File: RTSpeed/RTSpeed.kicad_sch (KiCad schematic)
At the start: 40 parts, among them J1 SWD, J2 USB C Receptacle, J3 MOTOR, J4 POWER IN, SW1 NRST, SW2 BOOT0, SW3 USER, U4 STM32F411CEUx, U5 LM317, Y1 25MHz, Y2 32.768kHz

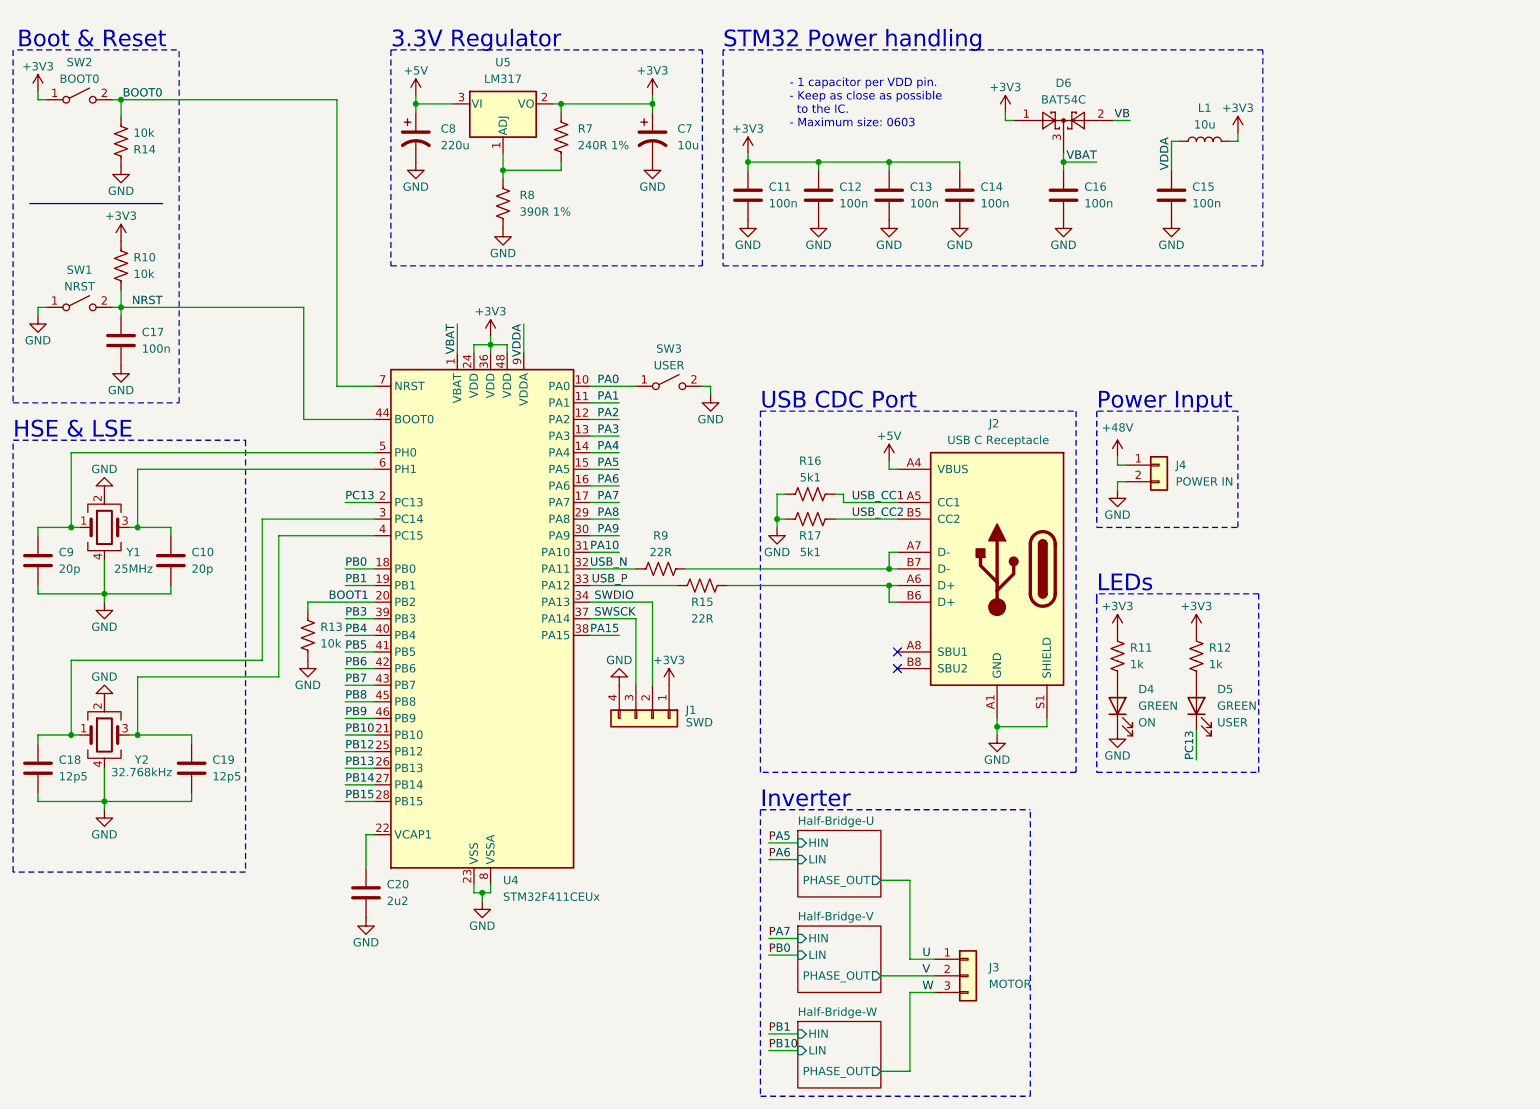
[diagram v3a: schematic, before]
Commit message: Added some footprints
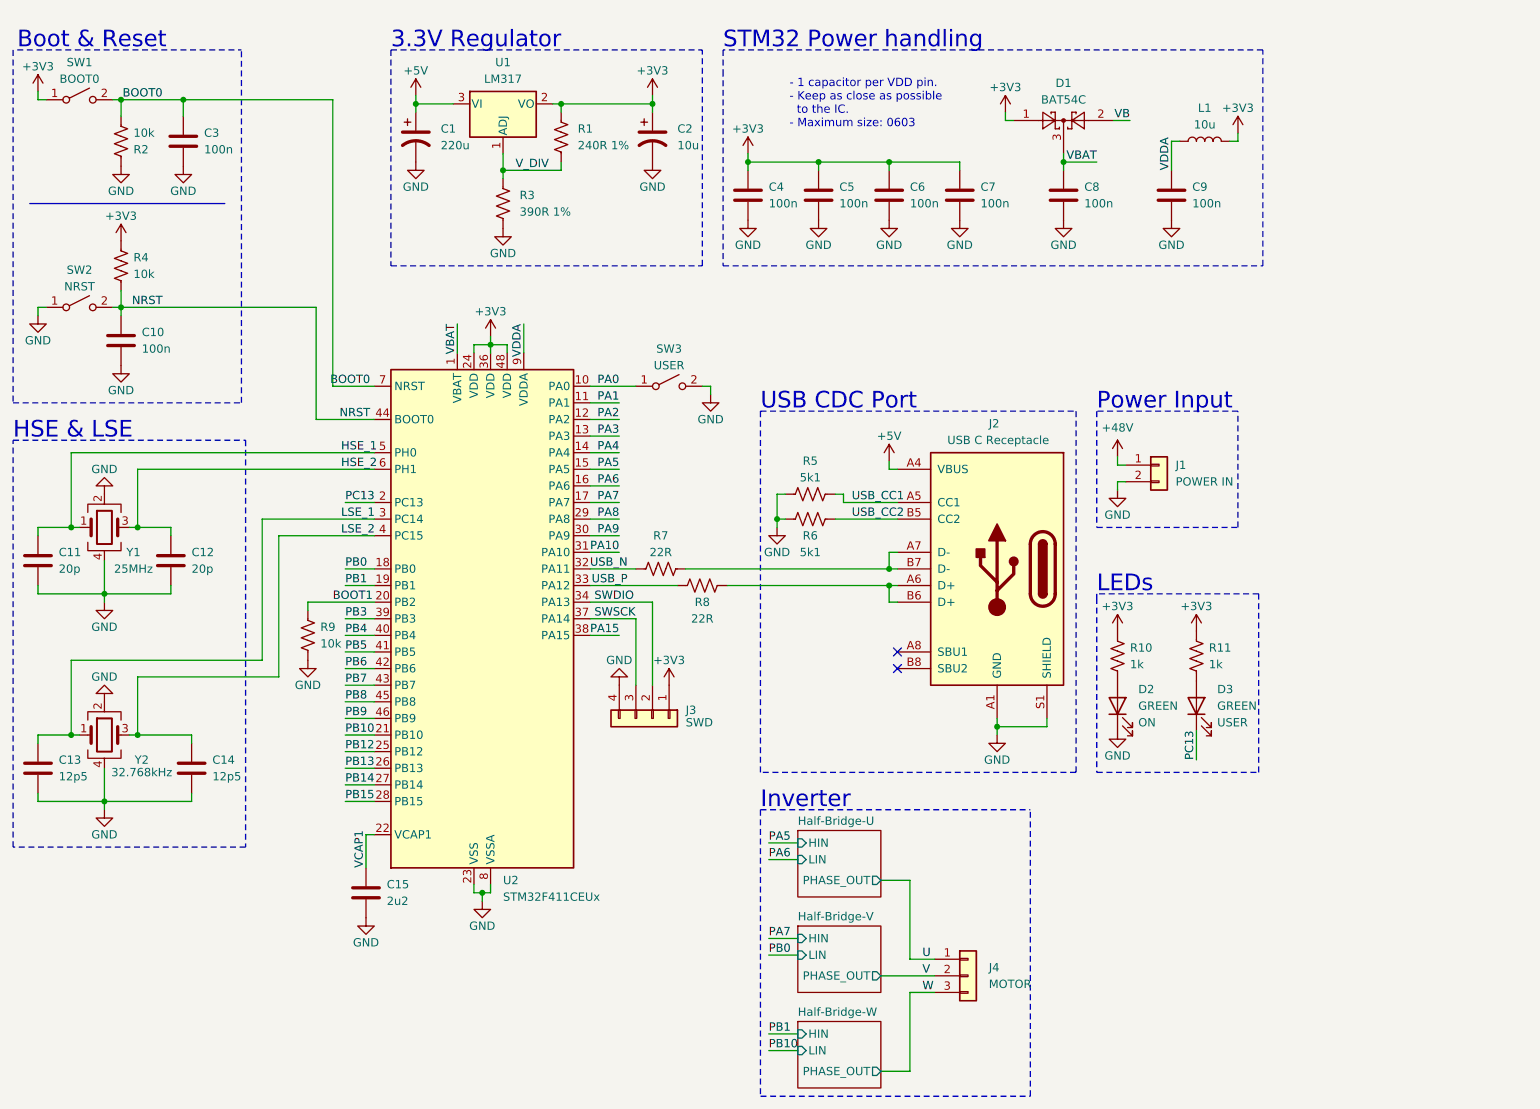
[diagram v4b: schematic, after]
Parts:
- added C3: 100n, Capacitor_SMD:C_0603_1608Metric, symbol Device:C
- C1: renamed from C8; footprint (none) -> Capacitor_THT:CP_Radial_D5.0mm_P2.00mm
- C10: renamed from C17; footprint (none) -> Capacitor_SMD:C_0603_1608Metric
- C11: renamed from C9; footprint (none) -> Capacitor_SMD:C_0603_1608Metric
- C12: renamed from C10; footprint (none) -> Capacitor_SMD:C_0603_1608Metric
- C13: renamed from C18; footprint (none) -> Capacitor_SMD:C_0603_1608Metric
- C14: renamed from C19; footprint (none) -> Capacitor_SMD:C_0603_1608Metric
- C15: renamed from C20; footprint (none) -> Capacitor_SMD:C_0603_1608Metric
- C2: renamed from C7; footprint (none) -> Capacitor_THT:CP_Radial_D5.0mm_P2.00mm
- C4: renamed from C11; footprint (none) -> Capacitor_SMD:C_0603_1608Metric
- C5: renamed from C12; footprint (none) -> Capacitor_SMD:C_0603_1608Metric
- C6: renamed from C13; footprint (none) -> Capacitor_SMD:C_0603_1608Metric
- C7: renamed from C14; footprint (none) -> Capacitor_SMD:C_0603_1608Metric
- C8: renamed from C16; footprint (none) -> Capacitor_SMD:C_0603_1608Metric
- C9: renamed from C15; footprint (none) -> Capacitor_SMD:C_0603_1608Metric
- D2: renamed from D4; footprint (none) -> LED_SMD:LED_0805_2012Metric
- D3: renamed from D5; footprint (none) -> LED_SMD:LED_0805_2012Metric
- J2: footprint (none) -> Connector_USB:USB_C_Receptacle_G-Switch_GT-USB-7010ASV
- J3: renamed from J1; footprint (none) -> Connector_PinHeader_2.54mm:PinHeader_1x04_P2.54mm_Vertical
- L1: footprint (none) -> Inductor_SMD:L_0805_2012Metric
- R1: renamed from R7; footprint (none) -> Resistor_SMD:R_0603_1608Metric
- R10: renamed from R11; footprint (none) -> Resistor_SMD:R_0603_1608Metric
- R11: renamed from R12; footprint (none) -> Resistor_SMD:R_0603_1608Metric
- R2: renamed from R14; footprint (none) -> Resistor_SMD:R_0603_1608Metric
- R3: renamed from R8; footprint (none) -> Resistor_SMD:R_0603_1608Metric
- R4: renamed from R10; footprint (none) -> Resistor_SMD:R_0603_1608Metric
- R5: renamed from R16; footprint (none) -> Resistor_SMD:R_0603_1608Metric
- R6: renamed from R17; footprint (none) -> Resistor_SMD:R_0603_1608Metric
- R7: renamed from R9; footprint (none) -> Resistor_SMD:R_0603_1608Metric
- R8: renamed from R15; footprint (none) -> Resistor_SMD:R_0603_1608Metric
- R9: renamed from R13; footprint (none) -> Resistor_SMD:R_0603_1608Metric
- SW1: renamed from SW2; footprint (none) -> Button_Switch_SMD:SW_Push_1P1T_NO_6x6mm_H9.5mm
- SW2: renamed from SW1; footprint (none) -> Button_Switch_SMD:SW_Push_1P1T_NO_6x6mm_H9.5mm
- SW3: footprint (none) -> Button_Switch_SMD:SW_Push_1P1T_NO_6x6mm_H9.5mm
- Y1, Y2: footprint (none) -> Oscillator:Oscillator_SMD_Abracon_ASE-4Pin_3.2x2.5mm
- renumbered D6 to D1, J4 to J1, J3 to J4, U5 to U1, U4 to U2
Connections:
- net BOOT0: now also C3.2
- net GND: now also C3.1
- net V_DIV: now reaches R1.2, R3.1, U1.1 (ADJ)
- net LSE_1: now reaches C13.1, U2.3 (PC14), Y2.1
- net LSE_2: now reaches C14.1, U2.4 (PC15), Y2.3
- net VCAP1: now reaches C15.1, U2.22 (VCAP1)
- net HSE_1: now reaches C11.1, U2.5 (PH0), Y1.1
- net HSE_2: now reaches C12.1, U2.6 (PH1), Y1.3
